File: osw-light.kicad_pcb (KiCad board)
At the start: 4 copper layers, 36.1 x 36.1 mm, 55 parts, among them J1 Conn_01x02, Q1 2N7002, SW1 SW_Push, SW2 SW_Push, SW4 SW_Push, SW5 SW_Push, U1 DS3231MZ, U10 XC6209, U11 MCP73831T-2ACI_OT, U13 XC6209, U2 BMA400, U4 GC9A01_IPS_display, U5 USB-OTG, U6 CH340E, U7 ttgo-32-micro, U9 TPS2115A

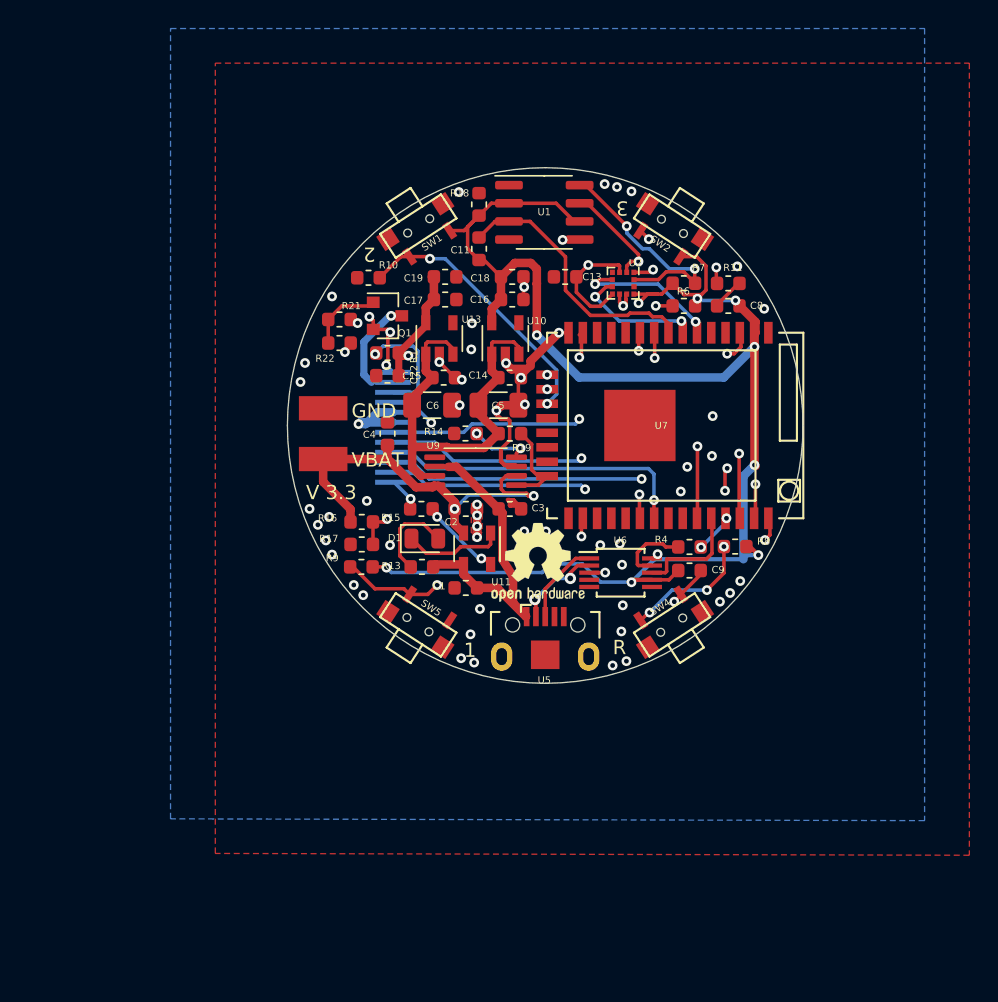
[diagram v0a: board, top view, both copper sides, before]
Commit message: added usb support
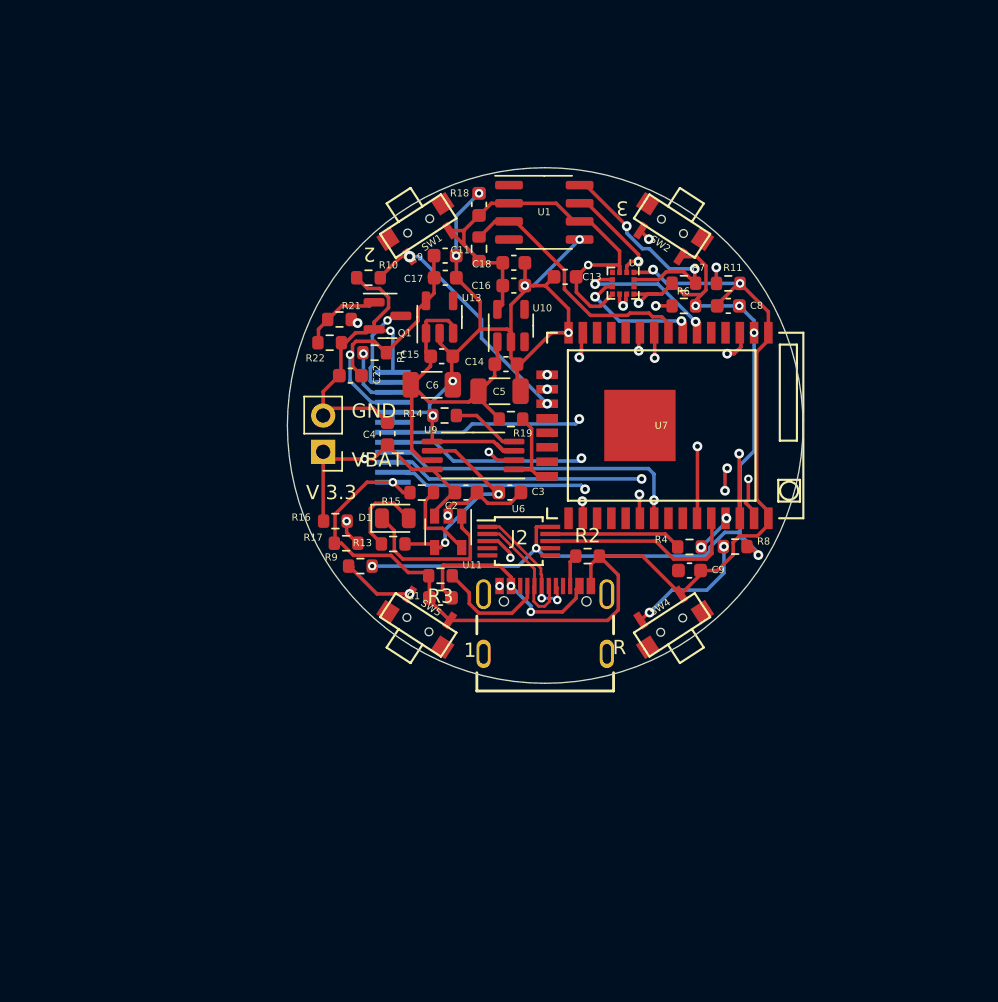
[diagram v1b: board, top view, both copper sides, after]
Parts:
- removed G***: LOGO, footprints:p3dt_tiny
- removed G***: LOGO, footprints:aisler_15x12mm
- removed REF**: OSHW-Logo2_7.3x6mm_SilkScreen, Symbol:OSHW-Logo2_7.3x6mm_SilkScreen
- removed REF**: KiCad-Logo2_5mm_SilkScreen, Symbol:KiCad-Logo2_5mm_SilkScreen
- removed U5: USB-OTG, open-Smartwatch:USBmicro-B
- added J2: USB_C_Receptacle_USB2.0, sat1l:GCT_USB4105-GF-A, F.Cu at (76.2, 117.6)
- added R2: 5.1k, Resistor_SMD:R_0603_1608Metric, F.Cu at (79.2, 110.8)
- added R3: 5.1k, Resistor_SMD:R_0603_1608Metric, F.Cu at (68.9, 112.1)
- moved U6 7.47 mm to (74.3, 109.7)
- moved C22 2.60 mm to (62.5, 98.1)
- moved R13 2.58 mm to (65.5, 109.9)
- moved D1 2.51 mm to (65.7, 108.1)
- moved U11 2.35 mm to (69.4, 109.0)
- moved R14 1.93 mm to (69.2, 100.9)
- moved C1 1.91 mm to (68.9, 113.7)
- moved R16 1.85 mm to (61.5, 108.3)
- moved C17 1.52 mm to (69.2, 91.2)
- moved U13 1.50 mm to (68.8, 94.0)
- moved C15 1.50 mm to (69.0, 96.8)
- moved C19 1.49 mm to (69.2, 89.7)
- moved C6 1.43 mm to (68.2, 98.8)
- moved R15 1.14 mm to (67.5, 106.3)
- moved C2 1.14 mm to (70.7, 106.3)
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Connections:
- U1 pad 1: Net-(U1-Pad1) -> unconnected-(U1-Pad1)
- U1 pad 4: Net-(U1-Pad4) -> unconnected-(U1-Pad4)
- U10 pad 4: Net-(U10-Pad4) -> unconnected-(U10-Pad4)
- U13 pad 4: Net-(U13-Pad4) -> unconnected-(U13-Pad4)
- U2 pad 11: Net-(U2-Pad11) -> unconnected-(U2-Pad11)
- U2 pad 4: Net-(U2-Pad4) -> unconnected-(U2-Pad4)
- U6 pad 4: Net-(U6-Pad4) -> unconnected-(U6-Pad4)
- U6 pad 5: Net-(U6-Pad5) -> unconnected-(U6-Pad5)
- U6 pad 6: Net-(U6-Pad6) -> unconnected-(U6-Pad6)
- U7 pad 11: Net-(U7-Pad11) -> unconnected-(U7-Pad11)
- U7 pad 12: Net-(U7-Pad12) -> unconnected-(U7-Pad12)
- U7 pad 13: Net-(U7-Pad13) -> unconnected-(U7-Pad13)
- U7 pad 19: Net-(U7-Pad19) -> unconnected-(U7-Pad19)
- U7 pad 20: Net-(U7-Pad20) -> unconnected-(U7-Pad20)
- U7 pad 21: Net-(U7-Pad21) -> unconnected-(U7-Pad21)
- U7 pad 22: Net-(U7-Pad22) -> unconnected-(U7-Pad22)
- U7 pad 24: Net-(U7-Pad24) -> unconnected-(U7-Pad24)
- U7 pad 26: Net-(U7-Pad26) -> unconnected-(U7-Pad26)
- U7 pad 27: Net-(U7-Pad27) -> unconnected-(U7-Pad27)
- U7 pad 28: Net-(U7-Pad28) -> unconnected-(U7-Pad28)
- U7 pad 31: Net-(U7-Pad31) -> unconnected-(U7-Pad31)
- U7 pad 32: Net-(U7-Pad32) -> unconnected-(U7-Pad32)
- U7 pad 4: Net-(U7-Pad4) -> unconnected-(U7-Pad4)
- U7 pad 5: Net-(U7-Pad5) -> unconnected-(U7-Pad5)
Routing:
- net GND: track 64.5 -> 209.6 mm, vias 65 -> 15
- net +3V3: track 126.3 -> 107.1 mm, vias 11 -> 8
- net /CC1: track 0.00 -> 8.06 mm
- net /VBUS: track 22.4 -> 29.9 mm, vias 0 -> 4
- net /RX: track 7.72 -> 14.5 mm
- net /VCC: track 30.7 -> 26.1 mm
- net Net-(D1-Pad1): track 7.01 -> 11.4 mm
- net Net-(R4-Pad1): track 5.10 -> 9.35 mm
- net Net-(R1-Pad2): track 7.87 -> 4.45 mm
- net /D_P: track 5.91 -> 9.24 mm, vias 0 -> 2
- net /FLASH: track 20.0 -> 23.0 mm
- net /3V3_2: track 17.5 -> 20.4 mm, vias 2 -> 1
- net /D_N: track 6.25 -> 9.10 mm, vias 2 -> 0
- net /CC2: track 0.00 -> 2.26 mm
- net /B_MON: track 26.9 -> 28.8 mm
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- removed copper zone on B.Cu, net GND
- removed copper zone on F.Cu, net GND
- removed copper zone on In1.Cu, net GND
- removed copper zone on In2.Cu, net GND
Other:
- net class Default removed

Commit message: some visual changes
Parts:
- moved R19 4.19 mm to (69.6, 100.8)
- moved D1 3.73 mm to (63.7, 105.0), turned to 90 degrees
- moved C6 3.05 mm to (65.2, 98.8)
- moved C5 2.67 mm to (70.4, 98.8)
- moved R14 2.62 mm to (66.5, 100.9)
- moved C14 2.36 mm to (71.2, 96.7)
- moved U9 2.20 mm to (69.0, 103.8)
- moved U11 2.16 mm to (67.2, 109.3)
- moved U6 2.04 mm to (72.3, 110.0)
- moved C16 2.02 mm to (76.0, 92.1)
- moved C18 2.02 mm to (76.0, 90.5)
- moved U10 2.00 mm to (72.6, 93.0)
- moved U7 1.84 mm to (83.0, 101.5)
- moved C13 1.74 mm to (79.2, 90.5)
- moved C4 1.65 mm to (63.6, 101.6)
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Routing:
- net GND: track 209.6 -> 0.00 mm, vias 15 -> 0
- net +3V3: track 107.1 -> 0.00 mm, vias 8 -> 0
- net /SCL: track 35.5 -> 0.00 mm, vias 3 -> 0
- net /VBUS: track 29.9 -> 0.00 mm, vias 4 -> 0
- net /TFT_RST: track 29.6 -> 0.00 mm, vias 2 -> 0
- net /B_MON: track 28.8 -> 0.00 mm, vias 2 -> 0
- net /VBAT: track 28.6 -> 0.00 mm, vias 2 -> 0
- net /MOSI: track 28.5 -> 0.00 mm, vias 2 -> 0
- net /SDA: track 28.4 -> 0.00 mm, vias 3 -> 0
- net /VCC: track 26.1 -> 0.00 mm
- net /EN: track 25.2 -> 0.00 mm, vias 5 -> 0
- net /FLASH: track 23.0 -> 0.00 mm, vias 2 -> 0
- net /BTN3: track 22.8 -> 0.00 mm, vias 3 -> 0
- net /SCK: track 22.0 -> 0.00 mm, vias 1 -> 0
- net /TFT_CS: track 20.6 -> 0.00 mm, vias 2 -> 0
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
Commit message: fixed some footprints and other stuff
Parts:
- moved R2 4.22 mm to (82.2, 112.9), turned to 90 degrees
- moved C9 0.22 mm to (86.3, 112.0)
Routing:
- net GND: track 0.00 -> 179.7 mm, vias 0 -> 18
- net +3V3: track 0.00 -> 104.0 mm, vias 0 -> 10
- net /VBUS: track 0.00 -> 37.5 mm, vias 0 -> 5
- net /VCC: track 0.00 -> 36.7 mm, vias 0 -> 2
- net /SCL: track 0.00 -> 30.9 mm, vias 0 -> 3
- net /VBAT: track 0.00 -> 28.1 mm
- net /MOSI: track 0.00 -> 27.7 mm, vias 0 -> 1
- net /B_MON: track 0.00 -> 26.2 mm, vias 0 -> 2
- net /SDA: track 0.00 -> 26.0 mm, vias 0 -> 3
- net /FLASH: track 0.00 -> 25.2 mm, vias 0 -> 2
- net /EN: track 0.00 -> 24.2 mm, vias 0 -> 3
- net /BTN3: track 0.00 -> 22.6 mm, vias 0 -> 2
- net /RTC_INT: track 0.00 -> 21.2 mm
- net /3V3_2: track 0.00 -> 20.3 mm, vias 0 -> 2
- net /SCK: track 0.00 -> 19.8 mm, vias 0 -> 1
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
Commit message: fixed routes here and there
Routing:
- net /B_MON: track 26.2 -> 53.0 mm, vias 2 -> 4
- net /BTN2: track 18.1 -> 22.7 mm
- net /RX: track 12.4 -> 14.8 mm
- net /PIN_LED: track 14.3 -> 16.5 mm
- net /BTN3: track 22.6 -> 24.2 mm
- net /VBUS: track 37.5 -> 36.6 mm
- net GND: track 179.7 -> 179.9 mm, vias 18 -> 56
- added copper zone on B.Cu, net GND
- added copper zone on F.Cu, net GND
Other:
- copper layers 4 -> 2

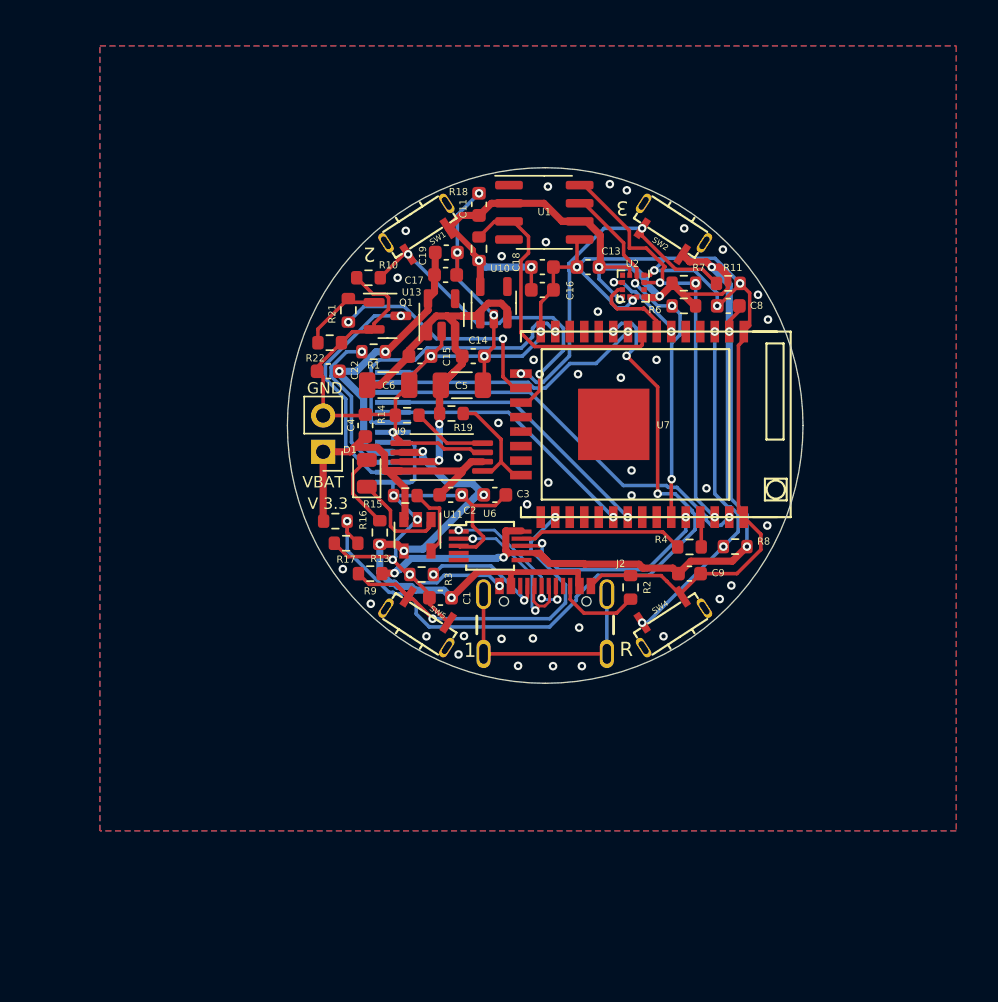
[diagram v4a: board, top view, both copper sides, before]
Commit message: Little fixes
now controller is not sticking out from the cpb, so it's (not)completely round, just before commiting i've realised that there is a display ribbon
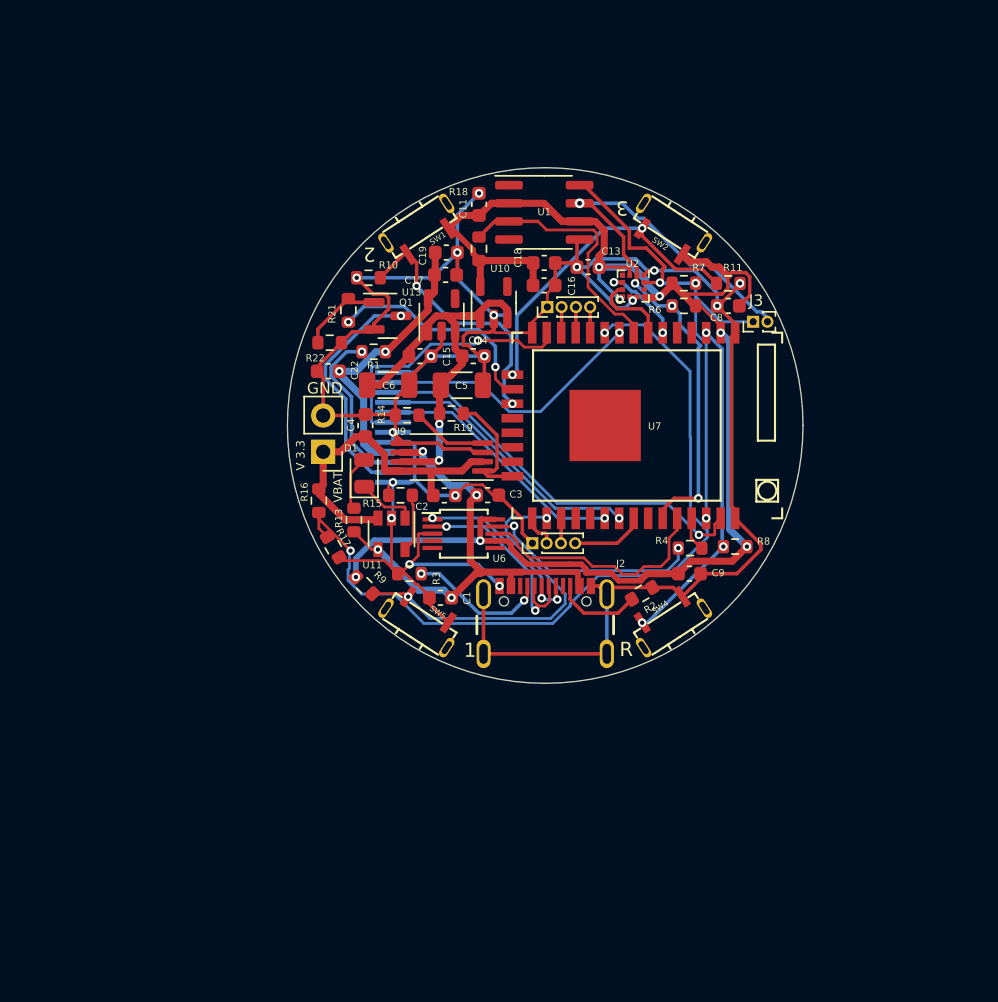
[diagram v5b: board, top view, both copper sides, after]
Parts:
- added J3: Conn_01x02, Connector_PinHeader_1.00mm:PinHeader_1x02_P1.00mm_Vertical, F.Cu at (90.8, 94.3)
- added J4: Conn_01x04, open-Smartwatch:PinHeader_1x04_P1.00mm_Vertical, F.Cu at (76.8, 109.8)
- added J5: Conn_01x04, open-Smartwatch:PinHeader_1x04_P1.00mm_Vertical, F.Cu at (77.8, 93.3)
- moved U6 2.03 mm to (70.5, 109.2)
- moved R13 2.01 mm to (62.8, 108.2)
- moved R16 1.84 mm to (60.3, 106.9), turned to -90 degrees
- moved U11 1.82 mm to (65.4, 109.2)
- moved R17 0.94 mm to (61.4, 110.1), turned to -60 degrees
- moved R9 0.92 mm to (63.5, 112.8), turned to -45 degrees
- moved R2 0.91 mm to (83.0, 113.4), turned to 30 degrees
- moved R3 0.85 mm to (66.7, 112.0)
- moved U7 0.61 mm to (82.4, 101.6)
- moved C3 0.50 mm to (72.2, 106.5)
- moved C2 0.45 mm to (69.1, 106.5)
- moved C16 0.34 mm to (76.1, 91.8)
- moved R15 0.34 mm to (66.1, 106.5)
- moved C18 0.32 mm to (76.1, 90.2)
- moved D1 0.18 mm to (63.5, 105.0)
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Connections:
- J2 pad S1: unconnected-(J2-PadS1) -> GND
- U7 pad 11: unconnected-(U7-Pad11) -> /GPIO06
- U7 pad 12: unconnected-(U7-Pad12) -> /GPIO27
- U7 pad 13: unconnected-(U7-Pad13) -> /GPIO14
- U7 pad 24: unconnected-(U7-Pad24) -> /GPIO02
- U7 pad 26: unconnected-(U7-Pad26) -> /GPIO04
- U7 pad 31: unconnected-(U7-Pad31) -> /GPIO19
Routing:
- net GND: track 179.9 -> 199.9 mm, vias 56 -> 17
- net /SDA: track 26.0 -> 45.5 mm, vias 3 -> 4
- net unconnected-(J2-PadS1): track 17.0 -> 0.00 mm
- net /SCL: track 30.9 -> 36.4 mm
- net /GPIO19: track 0.00 -> 5.18 mm
- net +3V3: track 103.7 -> 108.8 mm, vias 10 -> 7
- net /BTN2: track 22.7 -> 18.4 mm
- net Net-(R4-Pad1): track 11.6 -> 15.7 mm, vias 0 -> 2
- net /B_MON: track 53.0 -> 56.4 mm, vias 4 -> 2
- net /RTC_INT: track 21.2 -> 18.0 mm
- net Net-(D1-Pad1): track 7.16 -> 4.20 mm
- net /VBUS: track 36.6 -> 34.1 mm, vias 5 -> 4
- net /GPIO02: track 0.00 -> 2.44 mm
- net /VBAT: track 28.1 -> 25.6 mm
- net /D_P: track 11.6 -> 13.8 mm
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- removed copper zone on B.Cu, net GND
- removed copper zone on F.Cu, net GND
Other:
- board text removed: "P3DT.net"
- board text removed: "open-smartwatch.github.io"

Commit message: changed type-c to hro one, added cut on the edge for the display ribbon so everything can fit in r18.1mm circle
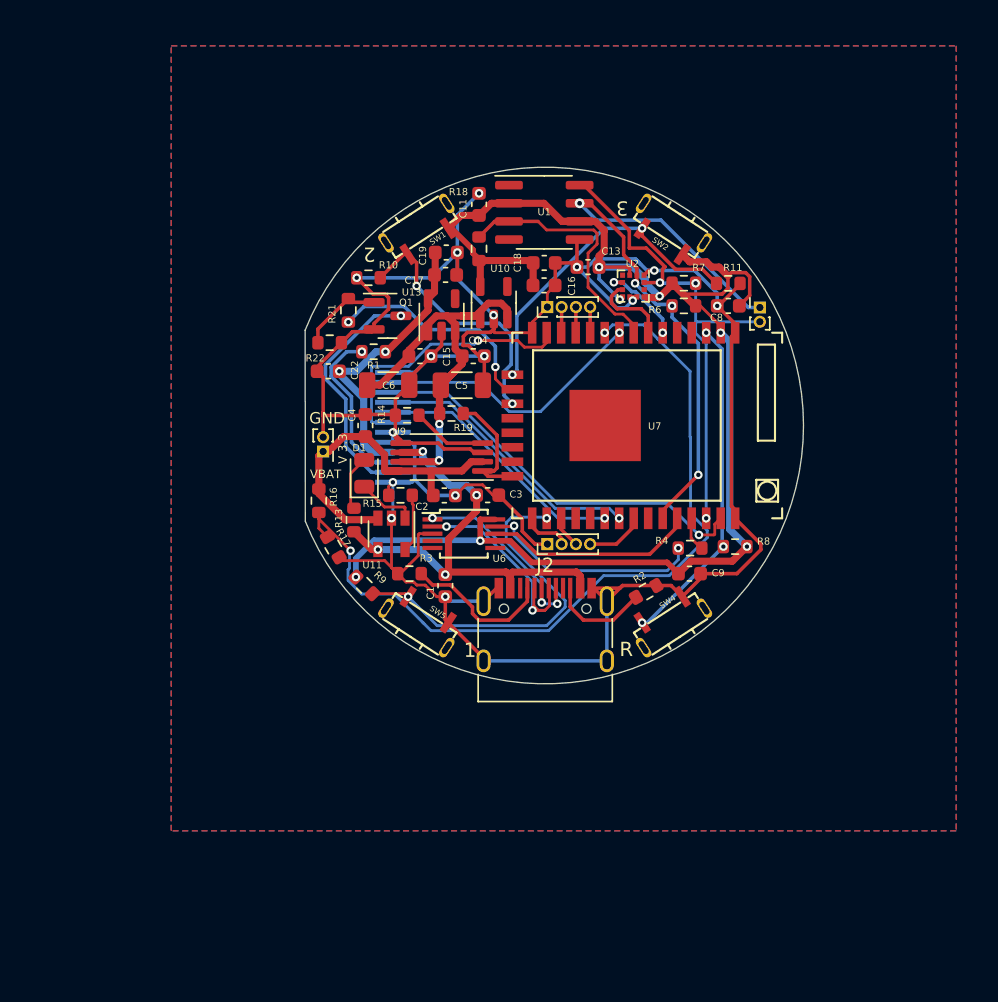
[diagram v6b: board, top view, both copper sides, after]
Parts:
- J1: footprint Connector_PinHeader_2.54mm:PinHeader_1x02_P2.54mm_Vertical -> open-Smartwatch:PinHeader_1x02_P1.0mm_Vertical
- J2: footprint sat1l:GCT_USB4105-GF-A -> Connector_USB:USB_C_Receptacle_HRO_TYPE-C-31-M-12
- J3: footprint Connector_PinHeader_1.00mm:PinHeader_1x02_P1.00mm_Vertical -> open-Smartwatch:PinHeader_1x02_P1.0mm_Vertical
- moved J4 1.05 mm to (77.8, 109.9)
- moved C1 0.92 mm to (69.2, 112.8), turned to 90 degrees
- moved J1 0.64 mm to (60.8, 102.8), turned to 90 degrees
- moved J2 0.56 mm to (76.2, 117.0)
- moved J3 0.51 mm to (91.1, 93.9), turned to -90 degrees
- moved R2 0.32 mm to (83.3, 113.2)
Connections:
- J3 pad 1: /SCL -> /SDA
- J3 pad 2: /SDA -> /SCL
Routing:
- net GND: track 199.9 -> 202.4 mm, vias 17 -> 15
- net /RX: track 17.0 -> 14.7 mm
- net /SDA: track 45.5 -> 43.9 mm
- net /SCL: track 36.4 -> 35.3 mm
- net /GPIO19: track 5.18 -> 4.15 mm
- net +3V3: track 108.8 -> 107.8 mm
- net /GPIO02: track 2.44 -> 3.39 mm
- net /CC2: track 6.06 -> 6.97 mm
- net /CC1: track 9.83 -> 10.5 mm, vias 2 -> 0
- net /VBUS: track 34.1 -> 33.5 mm
- net /FLASH: track 25.1 -> 25.6 mm
- added copper zone on B.Cu, net GND
- added copper zone on F.Cu, net GND
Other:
- board size 36.1 x 36.1 mm -> 34.9 x 36.2 mm

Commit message: added repo link on the watch
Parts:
- moved C1 12.7 mm to (62.0, 123.2)
- moved C11 12.7 mm to (64.3, 96.5)
- moved C17 12.7 mm to (62.0, 101.4)
- moved C18 12.7 mm to (68.9, 100.6)
- moved C22 12.7 mm to (53.8, 108.2)
- moved C4 12.7 mm to (56.4, 112.0)
- moved C6 12.7 mm to (58.0, 109.2)
- moved J1 12.7 mm to (53.6, 113.2)
- moved R11 12.7 mm to (81.8, 102.0)
- moved R14 12.7 mm to (59.3, 111.3)
- moved R15 12.7 mm to (58.8, 116.9)
- moved R2 12.7 mm to (76.0, 123.6)
- moved R22 12.7 mm to (53.9, 106.2)
- moved R9 12.7 mm to (56.3, 123.2)
- moved SW1 12.7 mm to (60.1, 98.0)
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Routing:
- net /IO34: track 6.06 -> 7.58 mm
- net /TFT_RST: track 19.0 -> 19.7 mm
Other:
- board text added: "github.com/ Sat1l/ open-smartwatch-light"
